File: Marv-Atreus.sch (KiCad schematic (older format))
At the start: 106 parts, among them SW1 SW_Push, U1 ATmega32U4-AU, Y1 16MHz

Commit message: First Proto
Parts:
- removed D26, D27: SOD-123, Diode_SMD:D_SOD-123, symbol Device:D_Small
- removed MX26, MX27: MX-NoLED, MX_Only:MXOnly-1U-NoLED, symbol MX_Alps_Hybrid:MX-NoLED
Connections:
- net Col0: now also U1.8 (PB0)
- net Col1: now also U1.9 (PB1)
- net Col10: now also U1.40 (PF1)
- net Col11: now also U1.41 (PF0)
- net Col2: now also U1.10 (PB2)
- net Col3: now also U1.11 (PB3)
- net Col4: now also U1.12 (PB7)
- net Col5: now also U1.22 (PD5)
- net Col6: now also U1.36 (PF7)
- net Col7: now also U1.37 (PF6)
- net Col8: now also U1.38 (PF5)
- net Col9: now also U1.39 (PF4)
- net Row0: now also U1.30 (PB6)
- net Row1: now also U1.29 (PB5)
- net Row2: now also U1.32 (PC7)
- net Row3: now also U1.31 (PC6)
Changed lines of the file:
@@
 	6750 5900 6850 5900
-$Comp
-L MX_Alps_Hybrid:MX-NoLED MX26
-U 1 1 5EA47DBA
-P 7400 5200
-F 0 "MX26" H 7433 5423 60  0000 C CNN
-F 1 "MX-NoLED" H 7433 5349 20  0000 C CNN
-F 2 "MX_Only:MXOnly-1U-NoLED" H 6775 5175 60  0001 C CNN
-F 3 "" H 6775 5175 60  0001 C CNN
-	1    7400 5200
-	1    0    0    -1
-$EndComp
-$Comp
-L Device:D_Small D26
-U 1 1 5EA47DC4
-P 7250 5450
-F 0 "D26" V 7296 5382 50  0000 R CNN
-F 1 "SOD-123" V 7205 5382 50  0000 R CNN
-F 2 "Diode_SMD:D_SOD-123" V 7250 5450 50  0001 C CNN
-F 3 "~" V 7250 5450 50  0001 C CNN
-	1    7250 5450
-	0    -1   -1   0
-$EndComp
-Wire Wire Line
-	7250 5350 7350 5350
 $Comp
 L MX_Alps_Hybrid:MX-NoLED MX38
@@
 	8550 5900 8650 5900
 $Comp
-L MX_Alps_Hybrid:MX-NoLED MX27
-U 1 1 5EA954FD
-P 8200 5200
-F 0 "MX27" H 8233 5423 60  0000 C CNN
-F 1 "MX-NoLED" H 8233 5349 20  0000 C CNN
-F 2 "MX_Only:MXOnly-1U-NoLED" H 7575 5175 60  0001 C CNN
-F 3 "" H 7575 5175 60  0001 C CNN
-	1    8200 5200
-	1    0    0    -1
-$EndComp
-$Comp
-L Device:D_Small D27
-U 1 1 5EA95507
-P 8050 5450
-F 0 "D27" V 8096 5382 50  0000 R CNN
-F 1 "SOD-123" V 8005 5382 50  0000 R CNN
-F 2 "Diode_SMD:D_SOD-123" V 8050 5450 50  0001 C CNN
-F 3 "~" V 8050 5450 50  0001 C CNN
-	1    8050 5450
-	0    -1   -1   0
-$EndComp
-Wire Wire Line
-	8050 5350 8150 5350
-$Comp
 L MX_Alps_Hybrid:MX-NoLED MX39
 U 1 1 5EA95512
@@
 Wire Wire Line
 	6750 5550 6250 5550
-Connection ~ 7250 5550
-Wire Wire Line
-	7250 5550 6750 5550
-Connection ~ 8050 5550
-Wire Wire Line
-	8050 5550 7250 5550
 Connection ~ 8550 5550
-Wire Wire Line
-	8550 5550 8050 5550
 Connection ~ 9050 5550
 Wire Wire Line
@@
 Wire Wire Line
 	7050 5150 7050 4600
-Wire Wire Line
-	7550 5700 7550 5150
-Connection ~ 7550 5150
-Wire Wire Line
-	7550 5150 7550 3800
-Wire Wire Line
-	8350 5700 8350 5150
-Connection ~ 8350 5150
-Wire Wire Line
-	8350 5150 8350 3800
 Wire Wire Line
 	8850 5700 8850 5150
@@
 Text GLabel 10850 3800 1    50   Input ~ 0
 Col11
+Wire Wire Line
+	7550 3800 7550 5700
+Wire Wire Line
+	8350 3800 8350 5700
+Wire Wire Line
+	6750 5550 8550 5550
+Text GLabel 3650 4100 2    50   Input ~ 0
+Col6
+Text GLabel 3650 3900 2    50   Input ~ 0
+Col8
+Text GLabel 3650 3800 2    50   Input ~ 0
+Col9
+Text GLabel 3650 3700 2    50   Input ~ 0
+Col10
+Text GLabel 3650 4000 2    50   Input ~ 0
+Col7
+Text GLabel 3650 3600 2    50   Input ~ 0
+Col11
+Text GLabel 3650 1200 2    50   Input ~ 0
+Col0
+Text GLabel 3650 1300 2    50   Input ~ 0
+Col1
+Text GLabel 3650 1400 2    50   Input ~ 0
+Col2
+Text GLabel 3650 1500 2    50   Input ~ 0
+Col3
+Text GLabel 3650 1900 2    50   Input ~ 0
+Col4
+Text GLabel 3650 2900 2    50   Input ~ 0
+Col5
+Text GLabel 3650 1700 2    50   Input ~ 0
+Row1
+Text GLabel 3650 1800 2    50   Input ~ 0
+Row0
+Text GLabel 3650 2100 2    50   Input ~ 0
+Row3
+Text GLabel 3650 2200 2    50   Input ~ 0
+Row2
 $EndSCHEMATC

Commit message: Rerotued the board
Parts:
- C1, C2, C3, C4, C5, C6, C7: footprint Capacitor_SMD:C_0805_2012Metric -> Capacitor_SMD:C_0603_1608Metric
- R1, R2, R3, R4, R5, R6: footprint Resistor_SMD:R_0805_2012Metric -> Resistor_SMD:R_0603_1608Metric
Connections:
- net Col0: now also MX10.1 (COL), MX20.1 (COL), MX32.1 (COL), MX44.1 (COL), U1.36 (PF7); no longer MX1.1 (COL), MX11.1 (COL), MX21.1 (COL), MX33.1 (COL), U1.8 (PB0)
- net Col1: now also MX19.1 (COL), MX31.1 (COL), MX43.1 (COL), MX9.1 (COL), U1.37 (PF6); no longer MX12.1 (COL), MX2.1 (COL), MX22.1 (COL), MX34.1 (COL), U1.9 (PB1)
- net Col10: now also MX12.1 (COL), MX2.1 (COL), MX22.1 (COL), MX34.1 (COL), U1.21 (PD3); no longer MX19.1 (COL), MX31.1 (COL), MX43.1 (COL), MX9.1 (COL), U1.40 (PF1)
- net Col11: now also MX1.1 (COL), MX11.1 (COL), MX21.1 (COL), MX33.1 (COL), U1.22 (PD5); no longer MX10.1 (COL), MX20.1 (COL), MX32.1 (COL), MX44.1 (COL), U1.41 (PF0)
- net Col2: now also MX18.1 (COL), MX30.1 (COL), MX42.1 (COL), MX8.1 (COL), U1.38 (PF5); no longer MX13.1 (COL), MX23.1 (COL), MX3.1 (COL), MX35.1 (COL), U1.10 (PB2)
- net Col3: now also MX17.1 (COL), MX29.1 (COL), MX41.1 (COL), MX7.1 (COL), U1.39 (PF4); no longer MX14.1 (COL), MX24.1 (COL), MX36.1 (COL), MX4.1 (COL), U1.11 (PB3)
- net Col4: now also MX16.1 (COL), MX28.1 (COL), MX40.1 (COL), MX6.1 (COL), U1.40 (PF1); no longer MX15.1 (COL), MX25.1 (COL), MX37.1 (COL), MX5.1 (COL), U1.12 (PB7)
- net Col5: now also MX39.1 (COL), U1.26 (PD6); no longer MX38.1 (COL), U1.22 (PD5)
- net Col6: now also MX38.1 (COL), U1.25 (PD4); no longer MX39.1 (COL), U1.36 (PF7)
- net Col7: now also MX15.1 (COL), MX25.1 (COL), MX37.1 (COL), MX5.1 (COL), U1.18 (PD0); no longer MX16.1 (COL), MX28.1 (COL), MX40.1 (COL), MX6.1 (COL), U1.37 (PF6)
- net Col8: now also MX14.1 (COL), MX24.1 (COL), MX36.1 (COL), MX4.1 (COL), U1.19 (PD1); no longer MX17.1 (COL), MX29.1 (COL), MX41.1 (COL), MX7.1 (COL), U1.38 (PF5)
- net Col9: now also MX13.1 (COL), MX23.1 (COL), MX3.1 (COL), MX35.1 (COL), U1.20 (PD2); no longer MX18.1 (COL), MX30.1 (COL), MX42.1 (COL), MX8.1 (COL), U1.39 (PF4)
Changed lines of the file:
@@
 F 0 "R6" V 4004 3300 50  0000 C CNN
 F 1 "10k" V 4095 3300 50  0000 C CNN
-F 2 "Resistor_SMD:R_0805_2012Metric" H 4200 3300 50  0001 C CNN
+F 2 "Resistor_SMD:R_0603_1608Metric" H 4200 3300 50  0001 C CNN
 F 3 "~" H 4200 3300 50  0001 C CNN
 	1    4200 3300
@@
 F 0 "R4" V 1854 2200 50  0000 C CNN
 F 1 "22" V 1945 2200 50  0000 C CNN
-F 2 "Resistor_SMD:R_0805_2012Metric" H 2050 2200 50  0001 C CNN
+F 2 "Resistor_SMD:R_0603_1608Metric" H 2050 2200 50  0001 C CNN
 F 3 "~" H 2050 2200 50  0001 C CNN
 	1    2050 2200
@@
 F 0 "R5" V 1504 2300 50  0000 C CNN
 F 1 "22" V 1595 2300 50  0000 C CNN
-F 2 "Resistor_SMD:R_0805_2012Metric" H 1700 2300 50  0001 C CNN
+F 2 "Resistor_SMD:R_0603_1608Metric" H 1700 2300 50  0001 C CNN
 F 3 "~" H 1700 2300 50  0001 C CNN
 	1    1700 2300
@@
 F 0 "C3" H 2142 2646 50  0000 L CNN
 F 1 "1uF" H 2142 2555 50  0000 L CNN
-F 2 "Capacitor_SMD:C_0805_2012Metric" H 2050 2600 50  0001 C CNN
+F 2 "Capacitor_SMD:C_0603_1608Metric" H 2050 2600 50  0001 C CNN
 F 3 "~" H 2050 2600 50  0001 C CNN
 	1    2050 2600
@@
 F 0 "C5" H 1092 3596 50  0000 L CNN
 F 1 "0.1uF" H 1092 3505 50  0000 L CNN
-F 2 "Capacitor_SMD:C_0805_2012Metric" H 1000 3550 50  0001 C CNN
+F 2 "Capacitor_SMD:C_0603_1608Metric" H 1000 3550 50  0001 C CNN
 F 3 "~" H 1000 3550 50  0001 C CNN
 	1    1000 3550
@@
 F 0 "C4" H 692 3596 50  0000 L CNN
 F 1 "0.1uF" H 692 3505 50  0000 L CNN
-F 2 "Capacitor_SMD:C_0805_2012Metric" H 600 3550 50  0001 C CNN
+F 2 "Capacitor_SMD:C_0603_1608Metric" H 600 3550 50  0001 C CNN
 F 3 "~" H 600 3550 50  0001 C CNN
 	1    600  3550
@@
 F 0 "C6" H 1492 3596 50  0000 L CNN
 F 1 "0.1uF" H 1492 3505 50  0000 L CNN
-F 2 "Capacitor_SMD:C_0805_2012Metric" H 1400 3550 50  0001 C CNN
+F 2 "Capacitor_SMD:C_0603_1608Metric" H 1400 3550 50  0001 C CNN
 F 3 "~" H 1400 3550 50  0001 C CNN
 	1    1400 3550
@@
 F 0 "C7" H 1892 3596 50  0000 L CNN
 F 1 "10uF" H 1892 3505 50  0000 L CNN
-F 2 "Capacitor_SMD:C_0805_2012Metric" H 1800 3550 50  0001 C CNN
+F 2 "Capacitor_SMD:C_0603_1608Metric" H 1800 3550 50  0001 C CNN
 F 3 "~" H 1800 3550 50  0001 C CNN
 	1    1800 3550
@@
 F 0 "C1" V 1171 1350 50  0000 C CNN
 F 1 "22pF" V 1262 1350 50  0000 C CNN
-F 2 "Capacitor_SMD:C_0805_2012Metric" H 1400 1350 50  0001 C CNN
+F 2 "Capacitor_SMD:C_0603_1608Metric" H 1400 1350 50  0001 C CNN
 F 3 "~" H 1400 1350 50  0001 C CNN
 	1    1400 1350
@@
 F 0 "C2" V 1171 1700 50  0000 C CNN
 F 1 "22pF" V 1262 1700 50  0000 C CNN
-F 2 "Capacitor_SMD:C_0805_2012Metric" H 1400 1700 50  0001 C CNN
+F 2 "Capacitor_SMD:C_0603_1608Metric" H 1400 1700 50  0001 C CNN
 F 3 "~" H 1400 1700 50  0001 C CNN
 	1    1400 1700
@@
 F 0 "R1" H 2409 946 50  0000 L CNN
 F 1 "10k" H 2409 855 50  0000 L CNN
-F 2 "Resistor_SMD:R_0805_2012Metric" H 2350 900 50  0001 C CNN
+F 2 "Resistor_SMD:R_0603_1608Metric" H 2350 900 50  0001 C CNN
 F 3 "~" H 2350 900 50  0001 C CNN
 	1    2350 900
@@
 F 0 "R2" H 4959 1496 50  0000 L CNN
 F 1 "5.1k" H 4959 1405 50  0000 L CNN
-F 2 "Resistor_SMD:R_0805_2012Metric" H 4900 1450 50  0001 C CNN
+F 2 "Resistor_SMD:R_0603_1608Metric" H 4900 1450 50  0001 C CNN
 F 3 "~" H 4900 1450 50  0001 C CNN
 	1    4900 1450
@@
 F 0 "R3" H 4959 2096 50  0000 L CNN
 F 1 "5.1k" H 4959 2005 50  0000 L CNN
-F 2 "Resistor_SMD:R_0805_2012Metric" H 4900 2050 50  0001 C CNN
+F 2 "Resistor_SMD:R_0603_1608Metric" H 4900 2050 50  0001 C CNN
 F 3 "~" H 4900 2050 50  0001 C CNN
 	1    4900 2050
@@
 Row3
 Text GLabel 5050 3800 1    50   Input ~ 0
+Col11
+Text GLabel 5550 3800 1    50   Input ~ 0
+Col10
+Text GLabel 6050 3800 1    50   Input ~ 0
+Col9
+Text GLabel 6550 3800 1    50   Input ~ 0
+Col8
+Text GLabel 7050 3800 1    50   Input ~ 0
+Col7
+Text GLabel 7550 3800 1    50   Input ~ 0
+Col6
+Text GLabel 8350 3800 1    50   Input ~ 0
+Col5
+Text GLabel 8850 3800 1    50   Input ~ 0
+Col4
+Text GLabel 9350 3800 1    50   Input ~ 0
+Col3
+Text GLabel 9850 3800 1    50   Input ~ 0
+Col2
+Text GLabel 10350 3800 1    50   Input ~ 0
+Col1
+Text GLabel 10850 3800 1    50   Input ~ 0
 Col0
-Text GLabel 5550 3800 1    50   Input ~ 0
-Col1
-Text GLabel 6050 3800 1    50   Input ~ 0
-Col2
-Text GLabel 6550 3800 1    50   Input ~ 0
-Col3
-Text GLabel 7050 3800 1    50   Input ~ 0
-Col4
-Text GLabel 7550 3800 1    50   Input ~ 0
-Col5
-Text GLabel 8350 3800 1    50   Input ~ 0
-Col6
-Text GLabel 8850 3800 1    50   Input ~ 0
-Col7
-Text GLabel 9350 3800 1    50   Input ~ 0
-Col8
-Text GLabel 9850 3800 1    50   Input ~ 0
-Col9
-Text GLabel 10350 3800 1    50   Input ~ 0
-Col10
-Text GLabel 10850 3800 1    50   Input ~ 0
-Col11
 Wire Wire Line
 	7550 3800 7550 5700
@@
 Wire Wire Line
 	6750 5550 8550 5550
-Text GLabel 3650 4100 2    50   Input ~ 0
-Col6
-Text GLabel 3650 3900 2    50   Input ~ 0
-Col8
-Text GLabel 3650 3800 2    50   Input ~ 0
-Col9
-Text GLabel 3650 3700 2    50   Input ~ 0
-Col10
-Text GLabel 3650 4000 2    50   Input ~ 0
-Col7
-Text GLabel 3650 3600 2    50   Input ~ 0
-Col11
-Text GLabel 3650 1200 2    50   Input ~ 0
-Col0
-Text GLabel 3650 1300 2    50   Input ~ 0
-Col1
-Text GLabel 3650 1400 2    50   Input ~ 0
-Col2
-Text GLabel 3650 1500 2    50   Input ~ 0
-Col3
-Text GLabel 3650 1900 2    50   Input ~ 0
-Col4
-Text GLabel 3650 2900 2    50   Input ~ 0
-Col5
 Text GLabel 3650 1700 2    50   Input ~ 0
 Row1
@@
 Text GLabel 3650 2200 2    50   Input ~ 0
 Row2
+Text GLabel 3650 2900 2    50   Input ~ 0
+Col11
+Text GLabel 3650 2700 2    50   Input ~ 0
+Col10
+Text GLabel 3650 2600 2    50   Input ~ 0
+Col9
+Text GLabel 3650 2500 2    50   Input ~ 0
+Col8
+Text GLabel 3650 2400 2    50   Input ~ 0
+Col7
+Text GLabel 3650 3000 2    50   Input ~ 0
+Col5
+Text GLabel 3650 2800 2    50   Input ~ 0
+Col6
+Text GLabel 3650 4100 2    50   Input ~ 0
+Col0
+Text GLabel 3650 4000 2    50   Input ~ 0
+Col1
+Text GLabel 3650 3900 2    50   Input ~ 0
+Col2
+Text GLabel 3650 3800 2    50   Input ~ 0
+Col3
+Text GLabel 3650 3700 2    50   Input ~ 0
+Col4
 $EndSCHEMATC

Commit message: Complete reroute
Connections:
- net Col0: now also MX1.1 (COL), MX11.1 (COL), MX21.1 (COL), MX33.1 (COL); no longer MX10.1 (COL), MX20.1 (COL), MX32.1 (COL), MX44.1 (COL)
- net Col1: now also MX12.1 (COL), MX2.1 (COL), MX22.1 (COL), MX34.1 (COL); no longer MX19.1 (COL), MX31.1 (COL), MX43.1 (COL), MX9.1 (COL)
- net Col10: now also MX19.1 (COL), MX31.1 (COL), MX43.1 (COL), MX9.1 (COL); no longer MX12.1 (COL), MX2.1 (COL), MX22.1 (COL), MX34.1 (COL)
- net Col11: now also MX10.1 (COL), MX20.1 (COL), MX32.1 (COL), MX44.1 (COL); no longer MX1.1 (COL), MX11.1 (COL), MX21.1 (COL), MX33.1 (COL)
- net Col2: now also MX13.1 (COL), MX23.1 (COL), MX3.1 (COL), MX35.1 (COL); no longer MX18.1 (COL), MX30.1 (COL), MX42.1 (COL), MX8.1 (COL)
- net Col3: now also MX14.1 (COL), MX24.1 (COL), MX36.1 (COL), MX4.1 (COL); no longer MX17.1 (COL), MX29.1 (COL), MX41.1 (COL), MX7.1 (COL)
- net Col4: now also MX15.1 (COL), MX25.1 (COL), MX37.1 (COL), MX5.1 (COL); no longer MX16.1 (COL), MX28.1 (COL), MX40.1 (COL), MX6.1 (COL)
- net Col5: now also MX38.1 (COL); no longer MX39.1 (COL)
- net Col6: now also MX39.1 (COL); no longer MX38.1 (COL)
- net Col7: now also MX16.1 (COL), MX28.1 (COL), MX40.1 (COL), MX6.1 (COL); no longer MX15.1 (COL), MX25.1 (COL), MX37.1 (COL), MX5.1 (COL)
- net Col8: now also MX17.1 (COL), MX29.1 (COL), MX41.1 (COL), MX7.1 (COL); no longer MX14.1 (COL), MX24.1 (COL), MX36.1 (COL), MX4.1 (COL)
- net Col9: now also MX18.1 (COL), MX30.1 (COL), MX42.1 (COL), MX8.1 (COL); no longer MX13.1 (COL), MX23.1 (COL), MX3.1 (COL), MX35.1 (COL)
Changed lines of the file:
@@
 Row3
 Text GLabel 5050 3800 1    50   Input ~ 0
+Col0
+Text GLabel 5550 3800 1    50   Input ~ 0
+Col1
+Text GLabel 6050 3800 1    50   Input ~ 0
+Col2
+Text GLabel 6550 3800 1    50   Input ~ 0
+Col3
+Text GLabel 7050 3800 1    50   Input ~ 0
+Col4
+Text GLabel 7550 3800 1    50   Input ~ 0
+Col5
+Text GLabel 8350 3800 1    50   Input ~ 0
+Col6
+Text GLabel 8850 3800 1    50   Input ~ 0
+Col7
+Text GLabel 9350 3800 1    50   Input ~ 0
+Col8
+Text GLabel 9850 3800 1    50   Input ~ 0
+Col9
+Text GLabel 10350 3800 1    50   Input ~ 0
+Col10
+Text GLabel 10850 3800 1    50   Input ~ 0
 Col11
-Text GLabel 5550 3800 1    50   Input ~ 0
-Col10
-Text GLabel 6050 3800 1    50   Input ~ 0
-Col9
-Text GLabel 6550 3800 1    50   Input ~ 0
-Col8
-Text GLabel 7050 3800 1    50   Input ~ 0
-Col7
-Text GLabel 7550 3800 1    50   Input ~ 0
-Col6
-Text GLabel 8350 3800 1    50   Input ~ 0
-Col5
-Text GLabel 8850 3800 1    50   Input ~ 0
-Col4
-Text GLabel 9350 3800 1    50   Input ~ 0
-Col3
-Text GLabel 9850 3800 1    50   Input ~ 0
-Col2
-Text GLabel 10350 3800 1    50   Input ~ 0
-Col1
-Text GLabel 10850 3800 1    50   Input ~ 0
-Col0
 Wire Wire Line
 	7550 3800 7550 5700

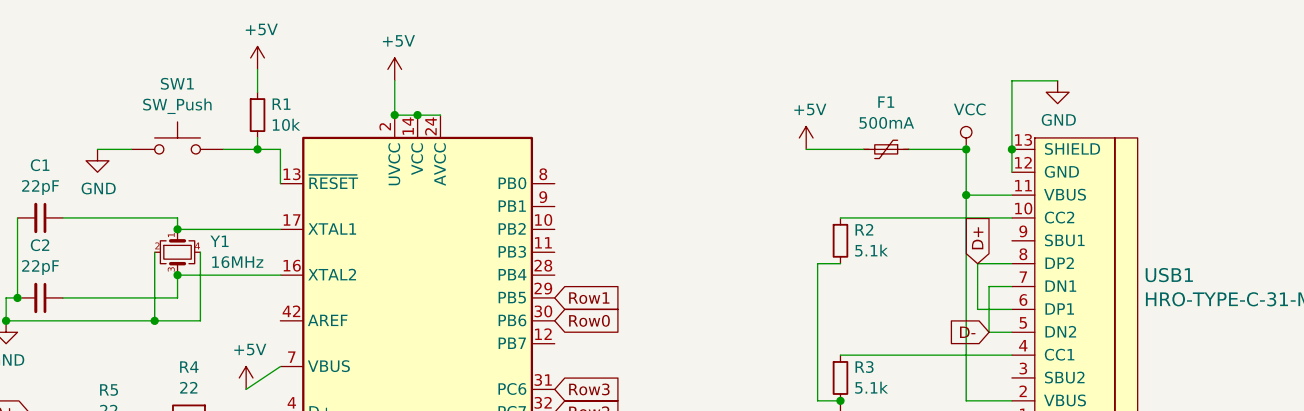
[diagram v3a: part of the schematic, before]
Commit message: Small Updates
- Decoupled USB Shield from GND
- Cap to GND as a LPF for the RST button
- Copper layer cleanup
- Rounded PCB corners
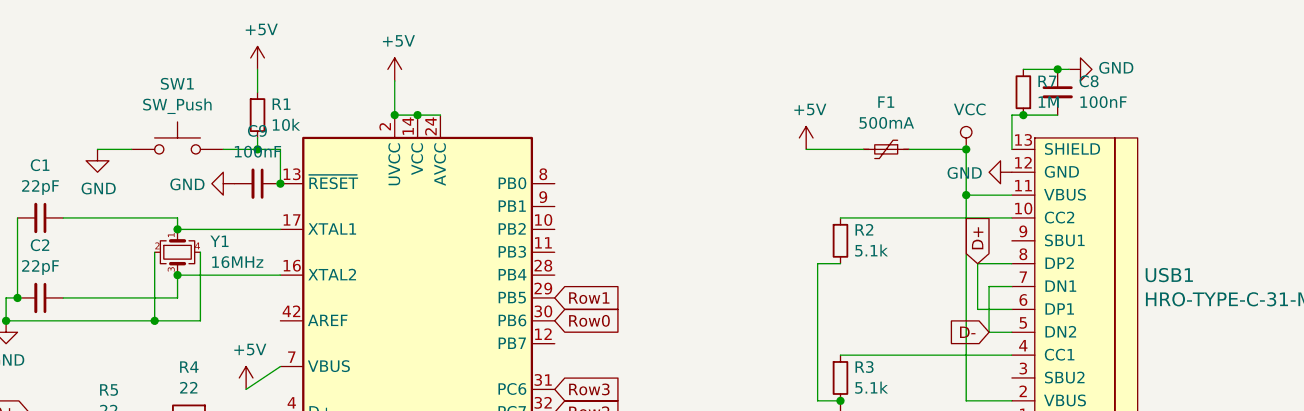
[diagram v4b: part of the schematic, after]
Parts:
- added C8, C9: 100nF, Capacitor_SMD:C_0603_1608Metric, symbol Device:C_Small
- added R7: 1M, Resistor_SMD:R_0603_1608Metric, symbol Device:R_Small
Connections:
- net GND: now also C8.1, C9.2, R7.2; no longer USB1.13 (SHIELD)
- net at R1.2, SW1.2, U1.13 (~RESET): now also C9.1
- new net: C8.2, R7.1, USB1.13 (SHIELD)
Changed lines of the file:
@@
 	5500 1550 5650 1550
-Wire Wire Line
-	5650 1050 5650 1150
 Wire Wire Line
 	5650 1250 5450 1250
@@
 	1    0    0    -1
 $EndComp
-$Comp
-L power:GND #PWR0113
-U 1 1 5EA10F57
-P 5850 750
-F 0 "#PWR0113" H 5850 500 50  0001 C CNN
-F 1 "GND" H 5855 577 50  0000 C CNN
-F 2 "" H 5850 750 50  0001 C CNN
-F 3 "" H 5850 750 50  0001 C CNN
-	1    5850 750
-	1    0    0    -1
-$EndComp
-Wire Wire Line
-	5650 1050 5650 750
-Wire Wire Line
-	5650 750  5850 750
-Connection ~ 5650 1050
 Text GLabel 5500 1550 1    50   Input ~ 0
 D+
@@
 Text GLabel 3650 3700 2    50   Input ~ 0
 Col4
+$Comp
+L Device:C_Small C9
+U 1 1 5E9FF33D
+P 2350 1200
+F 0 "C9" V 2121 1200 50  0000 C CNN
+F 1 "100nF" V 2212 1200 50  0000 C CNN
+F 2 "Capacitor_SMD:C_0603_1608Metric" H 2350 1200 50  0001 C CNN
+F 3 "~" H 2350 1200 50  0001 C CNN
+	1    2350 1200
+	0    1    1    0
+$EndComp
+Connection ~ 2450 1200
+$Comp
+L power:GND #PWR0113
+U 1 1 5EA004D9
+P 2250 1200
+F 0 "#PWR0113" H 2250 950 50  0001 C CNN
+F 1 "GND" V 2255 1072 50  0000 R CNN
+F 2 "" H 2250 1200 50  0001 C CNN
+F 3 "" H 2250 1200 50  0001 C CNN
+	1    2250 1200
+	0    1    1    0
+$EndComp
+$Comp
+L power:GND #PWR0116
+U 1 1 5EA0A2F8
+P 5650 1150
+F 0 "#PWR0116" H 5650 900 50  0001 C CNN
+F 1 "GND" V 5655 1022 50  0000 R CNN
+F 2 "" H 5650 1150 50  0001 C CNN
+F 3 "" H 5650 1150 50  0001 C CNN
+	1    5650 1150
+	0    1    1    0
+$EndComp
+$Comp
+L power:GND #PWR0117
+U 1 1 5EA0C030
+P 5900 700
+F 0 "#PWR0117" H 5900 450 50  0001 C CNN
+F 1 "GND" V 5905 572 50  0000 R CNN
+F 2 "" H 5900 700 50  0001 C CNN
+F 3 "" H 5900 700 50  0001 C CNN
+	1    5900 700
+	0    -1   -1   0
+$EndComp
+$Comp
+L Device:C_Small C8
+U 1 1 5EA0D5C9
+P 5850 800
+F 0 "C8" H 5942 846 50  0000 L CNN
+F 1 "100nF" H 5942 755 50  0000 L CNN
+F 2 "Capacitor_SMD:C_0603_1608Metric" H 5850 800 50  0001 C CNN
+F 3 "~" H 5850 800 50  0001 C CNN
+	1    5850 800
+	1    0    0    -1
+$EndComp
+Wire Wire Line
+	5650 1050 5650 900
+Wire Wire Line
+	5650 900  5700 900
+Wire Wire Line
+	5850 900  5700 900
+Connection ~ 5700 900
+Wire Wire Line
+	5700 700  5850 700
+Connection ~ 5850 700
+Wire Wire Line
+	5850 700  5900 700
+$Comp
+L Device:R_Small R7
+U 1 1 5EA0F42A
+P 5700 800
+F 0 "R7" H 5641 754 50  0000 R CNN
+F 1 "1M" H 5641 845 50  0000 R CNN
+F 2 "Resistor_SMD:R_0603_1608Metric" H 5700 800 50  0001 C CNN
+F 3 "~" H 5700 800 50  0001 C CNN
+	1    5700 800
+	-1   0    0    1
+$EndComp
 $EndSCHEMATC

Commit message: Even more Updates
- switched from Crystal to resonator
- added ESD protection ic
- Cleaned up silkscreen
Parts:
- removed C1, C2: 22pF, Capacitor_SMD:C_0603_1608Metric, symbol Device:C_Small
- removed Y1: 16MHz, Crystal:Crystal_SMD_3225-4Pin_3.2x2.5mm, symbol Device:Crystal_GND24_Small
- added U2: USBLC6-2SC6, Package_TO_SOT_SMD:SOT-23-6, symbol Power_Protection:USBLC6-2SC6
- added Y1: Resonator_Small, Crystal:Resonator_SMD_muRata_CSTxExxV-3Pin_3.0x1.1mm, symbol Device:Resonator_Small
- D1, D10, D11, D12, D13, D14, D15, D16, D17, D18, D19, D2, D20, D21, D22, D23, D24, D25, D28, D29, D3, D30, D31, D32, D33, D34, D35, D36, D37, D38, D39, D4, D40, D41, D42, D43, D44, D5, D6, D7, D8, D9: footprint Diode_SMD:D_SOD-123 -> random-keyboard-parts:D_SOD-123_NoReference
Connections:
- net D+: now also U2.3 (IO2); no longer R4.2
- net D-: now also U2.1 (IO1); no longer R5.2
- net GND: now also U2.2 (GND), Y1.2
- net VCC: now also U2.5 (VBUS)
- net at U1.16 (XTAL2): now also Y1.3
- net at U1.17 (XTAL1): now also Y1.1
- net at U1.3 (D-): now also R4.1; no longer R5.1
- net at U1.4 (D+): now also R5.1; no longer R4.1
- net LedSig: now reaches U1.41 (PF0)
- new net: R4.2, U2.6 (IO1)
- new net: R5.2, U2.4 (IO2)
